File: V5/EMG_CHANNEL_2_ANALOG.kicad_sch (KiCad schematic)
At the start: 38 parts, among them J401 AudioJack3 TRS, U401 INA333xxDGK, U402 MCP6004

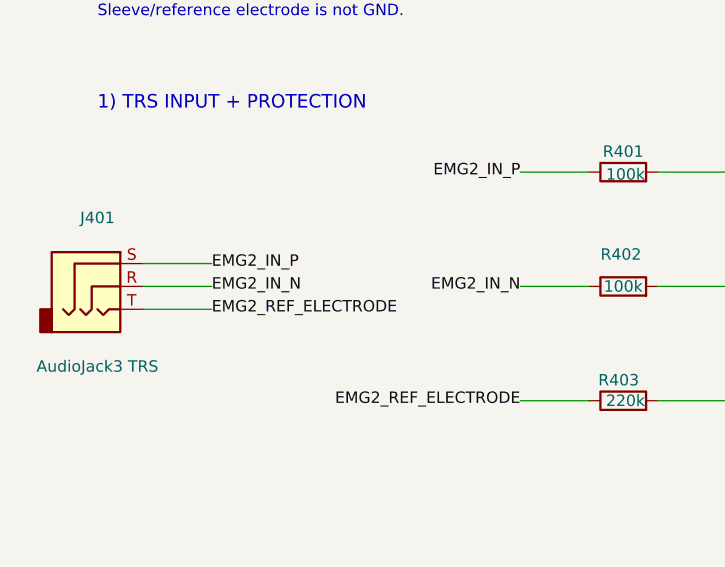
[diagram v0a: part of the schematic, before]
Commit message: fix trs electrode terminal mapping
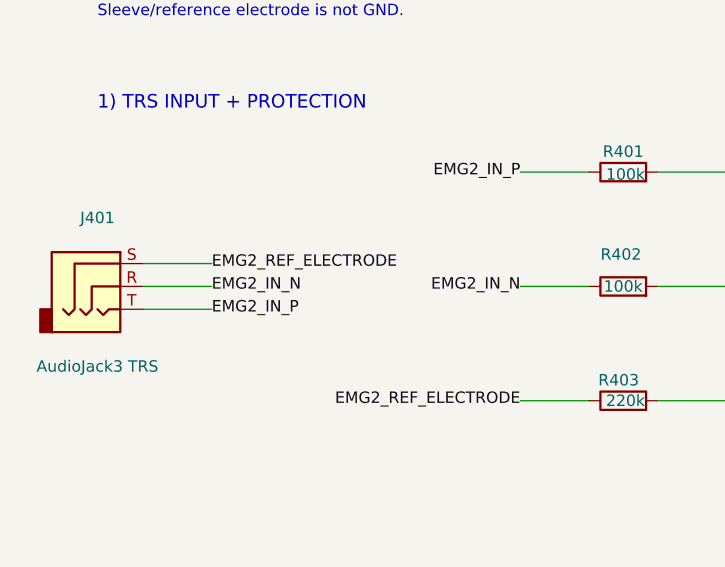
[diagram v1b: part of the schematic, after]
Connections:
- net EMG2_IN_P: now also J401.T; no longer J401.S
- net EMG2_REF_ELECTRODE: now also J401.S; no longer J401.T
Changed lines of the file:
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@@
 		)
 	)
-	(label "EMG2_IN_P"
+	(label "EMG2_REF_ELECTRODE"
 		(at 38.1 66.04 0)
 		(effects
@@
 		)
 	)
-	(label "EMG2_REF_ELECTRODE"
+	(label "EMG2_IN_P"
 		(at 38.1 71.12 0)
 		(effects

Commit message: assign mirrored analog footprint batch
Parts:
- C410, C411, C414: footprint (none) -> Capacitor_SMD:C_0603_1608Metric
- R411, R412, R413, R414, R421, R431, R441, R451: footprint (none) -> Resistor_SMD:R_0805_2012Metric
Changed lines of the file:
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@@
 			)
 		)
-		(property "Footprint" ""
+		(property "Footprint" "Capacitor_SMD:C_0603_1608Metric"
 			(at 195.58 58.42 0)
 			(hide yes)
@@
 			)
 		)
-		(property "Footprint" ""
+		(property "Footprint" "Capacitor_SMD:C_0603_1608Metric"
 			(at 246.38 73.66 0)
 			(hide yes)
@@
 			)
 		)
-		(property "Footprint" ""
+		(property "Footprint" "Resistor_SMD:R_0805_2012Metric"
 			(at 292.1 88.9 0)
 			(hide yes)
@@
 			)
 		)
-		(property "Footprint" ""
+		(property "Footprint" "Resistor_SMD:R_0805_2012Metric"
 			(at 302.26 107.95 0)
 			(hide yes)
@@
 			)
 		)
-		(property "Footprint" ""
+		(property "Footprint" "Resistor_SMD:R_0805_2012Metric"
 			(at 322.58 55.88 0)
 			(hide yes)
@@
 			)
 		)
-		(property "Footprint" ""
+		(property "Footprint" "Resistor_SMD:R_0805_2012Metric"
 			(at 365.76 73.66 0)
 			(hide yes)
@@
 			)
 		)
-		(property "Footprint" ""
+		(property "Footprint" "Capacitor_SMD:C_0603_1608Metric"
 			(at 434.34 78.74 0)
 			(hide yes)
@@
 			)
 		)
-		(property "Footprint" ""
+		(property "Footprint" "Resistor_SMD:R_0805_2012Metric"
 			(at 274.32 229.87 0)
 			(hide yes)
@@
 			)
 		)
-		(property "Footprint" ""
+		(property "Footprint" "Resistor_SMD:R_0805_2012Metric"
 			(at 438.15 57.15 0)
 			(hide yes)
@@
 			)
 		)
-		(property "Footprint" ""
+		(property "Footprint" "Resistor_SMD:R_0805_2012Metric"
 			(at 439.42 93.98 0)
 			(hide yes)
@@
 			)
 		)
-		(property "Footprint" ""
+		(property "Footprint" "Resistor_SMD:R_0805_2012Metric"
 			(at 436.88 119.38 0)
 			(hide yes)

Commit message: select and assign analog ic packages
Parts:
- U401: value INA333xxDGK -> INA333AIDGKT; footprint (none) -> Package_SO:VSSOP-8_3x3mm_P0.65mm
- U402: value MCP6004 -> MCP6004-I/SL; footprint Package_DIP:DIP-14_W7.62mm -> Package_SO:SOIC-14_3.9x8.7mm_P1.27mm
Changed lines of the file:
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@@
 			)
 		)
-		(property "Value" "INA333xxDGK"
+		(property "Value" "INA333AIDGKT"
 			(at 196.85 90.17 0)
 			(show_name no)
@@
 			)
 		)
-		(property "Footprint" ""
+		(property "Footprint" "Package_SO:VSSOP-8_3x3mm_P0.65mm"
 			(at 210.82 73.66 0)
 			(hide yes)
@@
 			)
 		)
-		(property "Value" "MCP6004"
+		(property "Value" "MCP6004-I/SL"
 			(at 322.58 80.518 0)
 			(show_name no)
@@
 			)
 		)
-		(property "Footprint" "Package_DIP:DIP-14_W7.62mm"
+		(property "Footprint" "Package_SO:SOIC-14_3.9x8.7mm_P1.27mm"
 			(at 322.58 73.66 0)
 			(hide yes)
@@
 			)
 		)
-		(property "Value" "MCP6004"
+		(property "Value" "MCP6004-I/SL"
 			(at 337.82 165.1 0)
 			(show_name no)
@@
 			)
 		)
-		(property "Footprint" "Package_DIP:DIP-14_W7.62mm"
+		(property "Footprint" "Package_SO:SOIC-14_3.9x8.7mm_P1.27mm"
 			(at 337.82 157.48 0)
 			(hide yes)
@@
 			)
 		)
-		(property "Value" "MCP6004"
+		(property "Value" "MCP6004-I/SL"
 			(at 337.312 236.982 0)
 			(show_name no)
@@
 			)
 		)
-		(property "Footprint" "Package_DIP:DIP-14_W7.62mm"
+		(property "Footprint" "Package_SO:SOIC-14_3.9x8.7mm_P1.27mm"
 			(at 337.82 229.87 0)
 			(hide yes)
@@
 			)
 		)
-		(property "Value" "MCP6004"
+		(property "Value" "MCP6004-I/SL"
 			(at 278.384 313.436 0)
 			(show_name no)
@@
 			)
 		)
-		(property "Footprint" "Package_DIP:DIP-14_W7.62mm"
+		(property "Footprint" "Package_SO:SOIC-14_3.9x8.7mm_P1.27mm"
 			(at 278.13 306.07 0)
 			(hide yes)
@@
 			)
 		)
-		(property "Value" "MCP6004"
+		(property "Value" "MCP6004-I/SL"
 			(at 419.608 178.054 0)
 			(show_name no)
@@
 			)
 		)
-		(property "Footprint" "Package_DIP:DIP-14_W7.62mm"
+		(property "Footprint" "Package_SO:SOIC-14_3.9x8.7mm_P1.27mm"
 			(at 420.37 165.1 0)
 			(hide yes)

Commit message: assign analog input filter footprints
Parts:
- C401, C402, C403: footprint (none) -> Capacitor_SMD:C_0603_1608Metric
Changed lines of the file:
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@@
 			)
 		)
-		(property "Footprint" ""
+		(property "Footprint" "Capacitor_SMD:C_0603_1608Metric"
 			(at 130.81 134.62 0)
 			(hide yes)
@@
 			)
 		)
-		(property "Footprint" ""
+		(property "Footprint" "Capacitor_SMD:C_0603_1608Metric"
 			(at 130.81 104.14 0)
 			(hide yes)
@@
 			)
 		)
-		(property "Footprint" ""
+		(property "Footprint" "Capacitor_SMD:C_0603_1608Metric"
 			(at 168.91 95.25 0)
 			(hide yes)

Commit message: retain footprints for optional dnp filters
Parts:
- C404: footprint (none) -> Capacitor_SMD:C_0603_1608Metric
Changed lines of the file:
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@@
 			)
 		)
-		(property "Footprint" ""
+		(property "Footprint" "Capacitor_SMD:C_0603_1608Metric"
 			(at 130.81 118.11 0)
 			(hide yes)

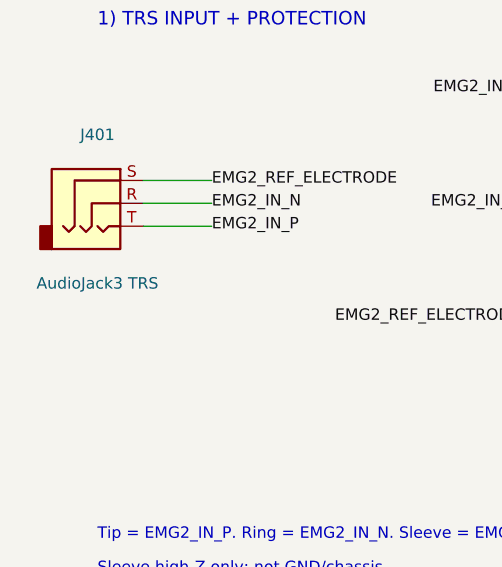
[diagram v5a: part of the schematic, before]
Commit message: select and assign mechanical interface parts
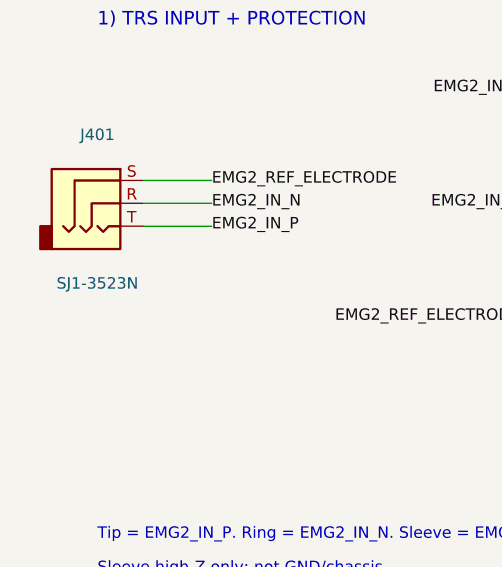
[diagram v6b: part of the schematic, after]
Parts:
- J401: value AudioJack3 TRS -> SJ1-3523N; footprint (none) -> Connector_Audio:Jack_3.5mm_CUI_SJ1-3523N_Horizontal
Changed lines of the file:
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@@
 			)
 		)
-		(property "Value" "AudioJack3 TRS"
+		(property "Value" "SJ1-3523N"
 			(at 25.4 77.47 0)
 			(show_name no)
@@
 			)
 		)
-		(property "Footprint" ""
+		(property "Footprint" "Connector_Audio:Jack_3.5mm_CUI_SJ1-3523N_Horizontal"
 			(at 25.4 68.58 0)
 			(hide yes)

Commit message: assign final resistor footprints
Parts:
- R401, R402, R403, R404, R405, R406: footprint (none) -> Resistor_SMD:R_1206_3216Metric
- R407: footprint (none) -> Resistor_SMD:R_0805_2012Metric
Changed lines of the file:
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@@
 			)
 		)
-		(property "Footprint" ""
+		(property "Footprint" "Resistor_SMD:R_1206_3216Metric"
 			(at 83.82 55.88 0)
 			(hide yes)
@@
 			)
 		)
-		(property "Footprint" ""
+		(property "Footprint" "Resistor_SMD:R_1206_3216Metric"
 			(at 83.82 68.58 0)
 			(hide yes)
@@
 			)
 		)
-		(property "Footprint" ""
+		(property "Footprint" "Resistor_SMD:R_1206_3216Metric"
 			(at 83.82 81.28 0)
 			(hide yes)
@@
 			)
 		)
-		(property "Footprint" ""
+		(property "Footprint" "Resistor_SMD:R_1206_3216Metric"
 			(at 130.81 57.15 0)
 			(hide yes)
@@
 			)
 		)
-		(property "Footprint" ""
+		(property "Footprint" "Resistor_SMD:R_1206_3216Metric"
 			(at 130.81 72.39 0)
 			(hide yes)
@@
 			)
 		)
-		(property "Footprint" ""
+		(property "Footprint" "Resistor_SMD:R_1206_3216Metric"
 			(at 130.81 87.63 0)
 			(hide yes)
@@
 			)
 		)
-		(property "Footprint" ""
+		(property "Footprint" "Resistor_SMD:R_0805_2012Metric"
 			(at 168.91 73.66 0)
 			(hide yes)

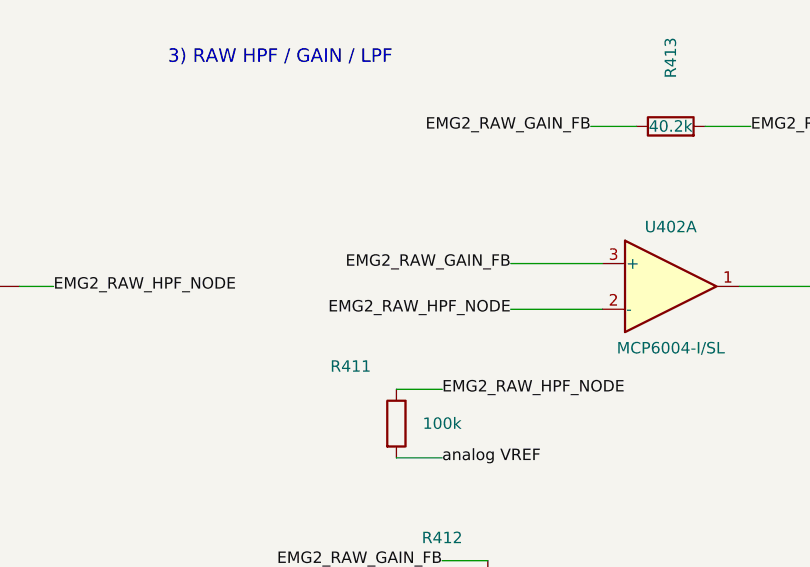
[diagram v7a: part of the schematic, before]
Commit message: Place EMG V5 PCB blocks and fix analog feedback nets
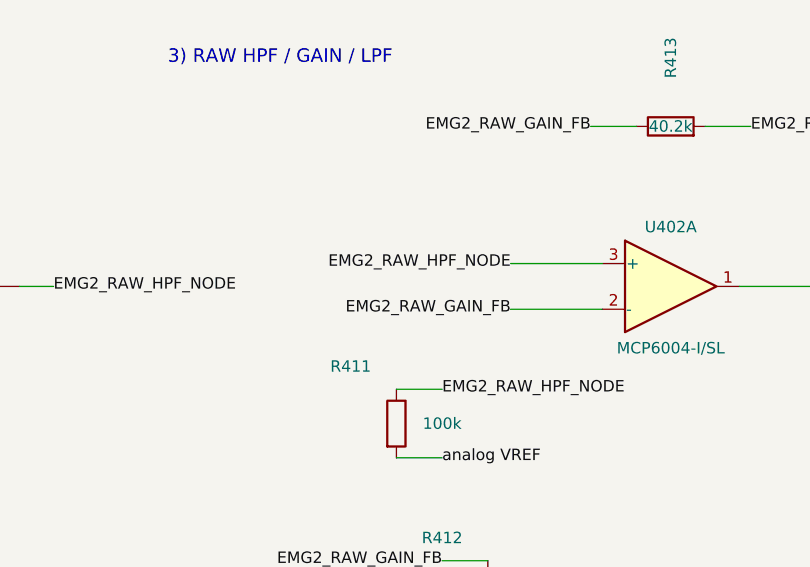
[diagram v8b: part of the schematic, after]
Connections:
- net EMG2_RAW_GAIN_FB: now also U402.2 (-); no longer U402.3 (+)
- net EMG2_RAW_HPF_NODE: now also U402.3 (+); no longer U402.2 (-)
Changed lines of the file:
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@@
 		)
 	)
-	(label "EMG2_RAW_HPF_NODE"
+	(label "EMG2_RAW_GAIN_FB"
 		(at 304.8 76.2 180)
 		(effects
@@
 		)
 	)
-	(label "EMG2_RAW_GAIN_FB"
+	(label "EMG2_RAW_HPF_NODE"
 		(at 304.8 71.12 180)
 		(effects
@@
 		)
 	)
-	(embedded_fonts no)
 )
